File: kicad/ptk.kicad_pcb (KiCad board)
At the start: 2 copper layers, 121 x 87.8 mm, 18 parts

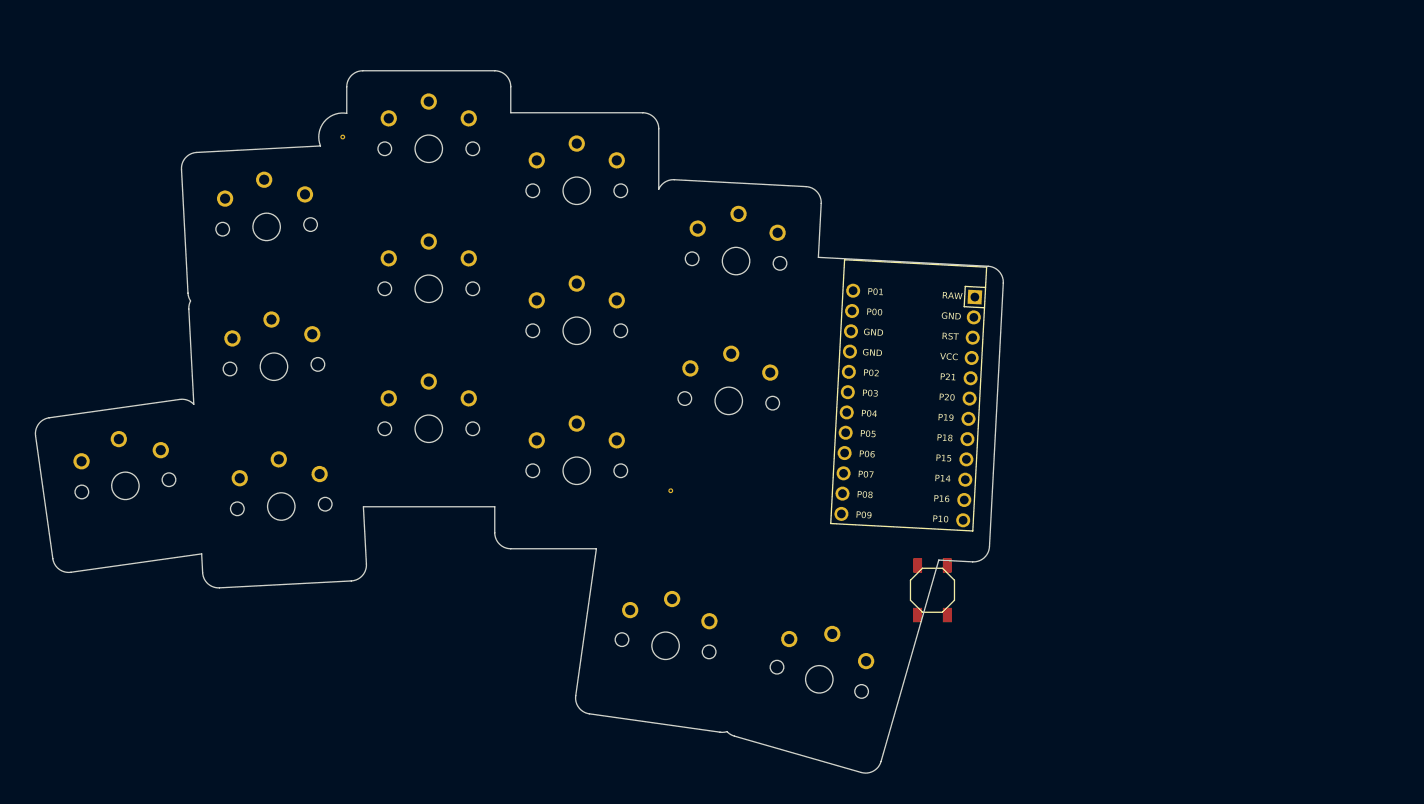
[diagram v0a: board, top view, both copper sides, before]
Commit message: updated schematic and footprints
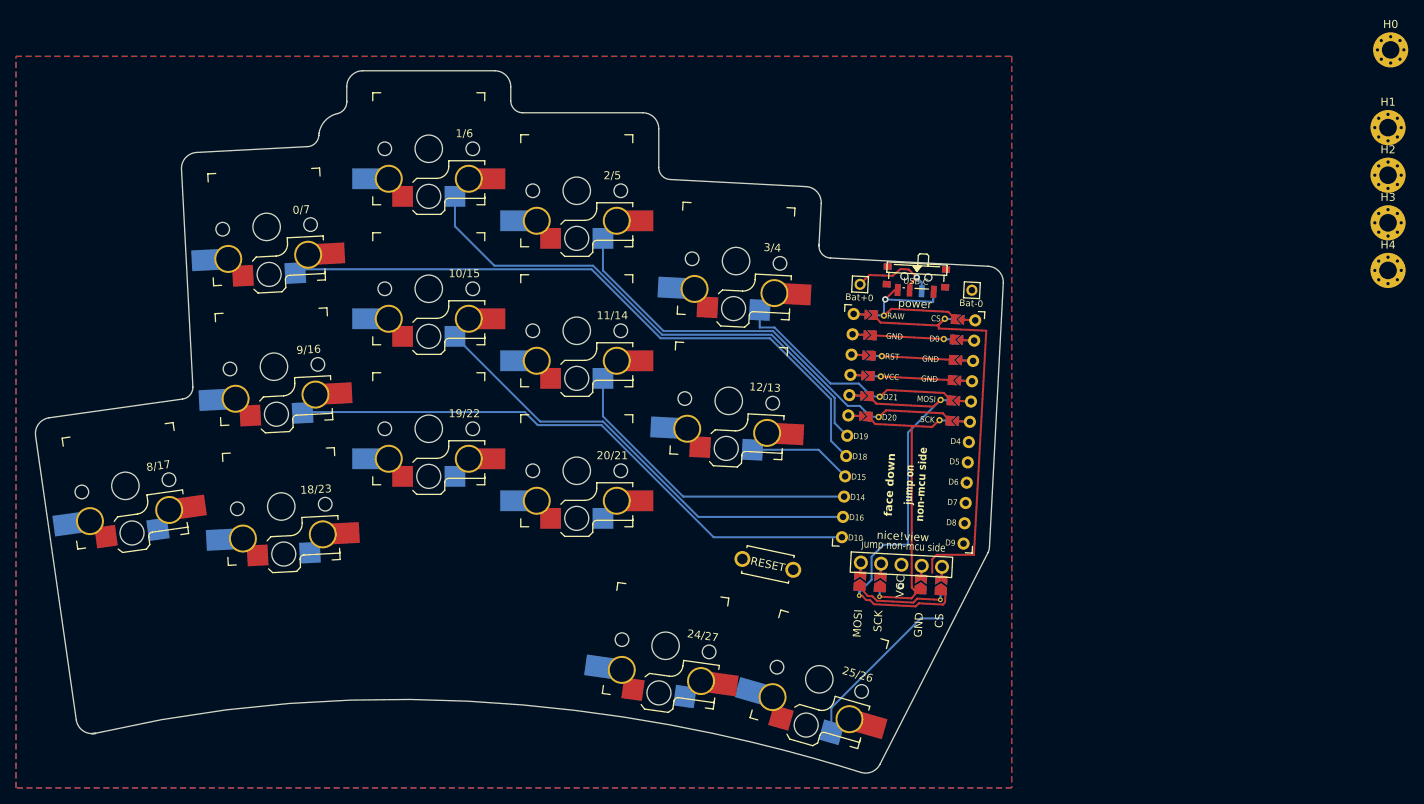
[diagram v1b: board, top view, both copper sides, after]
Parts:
- removed REF** (x2): VIA-0.6mm, VIA-0.6mm
- added Bat+0: MountingHole_Pad, keyboard:1pin_conn, F.Cu at (263.0, 114.9)
- added Bat-0: MountingHole_Pad, keyboard:1pin_conn, F.Cu at (277.0, 115.6)
- added H0: MountingHole_Pad, MountingHole:MountingHole_2.2mm_M2_Pad_Via, F.Cu at (329.3, 85.5)
- added H1: MountingHole_Pad, MountingHole:MountingHole_2.2mm_M2_Pad_Via, F.Cu at (329.0, 95.3)
- added H2: MountingHole_Pad, MountingHole:MountingHole_2.2mm_M2_Pad_Via, F.Cu at (329.0, 101.2)
- added H3: MountingHole_Pad, MountingHole:MountingHole_2.2mm_M2_Pad_Via, F.Cu at (329.0, 107.2)
- added H4: MountingHole_Pad, MountingHole:MountingHole_2.2mm_M2_Pad_Via, F.Cu at (329.0, 113.1)
- added J0: nice!view, chelming-kbd:nice-view_reversible, F.Cu at (269.0, 133.4)
- added RSW0: SW_Push, kbd:ResetSW, F.Cu at (251.5, 149.9)
- 0/7, 1/6, 10/15, 11/14, 12/13, 18/23, 19/22, 2/5, 20/21, 24/27, 25/26, 3/4, 8/17, 9/16: value (none) -> keyswitch; footprint PG1350 -> chelming-kbd:choc_v1_hotswap_reversible
- MCU0: renamed from MCU1; value (none) -> ProMicro-kbd; footprint ProMicro -> chelming-kbd:ProMicro_v3_nice_view_reversible
- SW_PWR0: renamed from B1; value (none) -> SW_SPST; footprint E73:SW_TACT_ALPS_SKQGABE010 -> chelming-kbd:SW_SPDT_PCM12_REVERSIBLE
- moved SW_PWR0 39.9 mm to (270.1, 113.2), turned to -3 degrees
- moved MCU0 3.42 mm to (269.0, 133.4), turned to -3 degrees
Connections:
- 0/7 pad 2: matrix_ring_top -> s0
- 1/6 pad 2: matrix_middle_top -> s1
- 10/15 pad 2: matrix_middle_home -> s10
- 11/14 pad 2: matrix_index_home -> s11
- 12/13 pad 2: matrix_inner_home -> s12
- 18/23 pad 2: matrix_ring_bottom -> s18
- 19/22 pad 2: matrix_middle_bottom -> s19
- 2/5 pad 2: matrix_index_top -> s2
- 20/21 pad 2: matrix_index_bottom -> s20
- 24/27 pad 2: thumb_tucky -> s24
- 25/26 pad 2: thumb_reachy -> s25
- 3/4 pad 2: matrix_inner_top -> s3
- 8/17 pad 2: matrix_pinky_home -> s8
- 9/16 pad 2: matrix_ring_home -> s9
- MCU0 pad 1: RAW -> cs
- MCU0 pad 10: matrix_middle_top -> s20
- MCU0 pad 11: matrix_middle_home -> s24
- MCU0 pad 12: matrix_middle_bottom -> s25
- MCU0 pad 13: P1 -> s9
- MCU0 pad 14: P0 -> s10
- MCU0 pad 15: GND -> s11
- MCU0 pad 16: GND -> s12
- MCU0 pad 17: P2 -> s0
- MCU0 pad 18: matrix_index_top -> s1
- MCU0 pad 19: matrix_index_home -> s2
- MCU0 pad 2: GND -> unconnected-(MCU0-RX-Pad2)_1
- MCU0 pad 20: matrix_index_bottom -> s3
- MCU0 pad 21: matrix_inner_top -> VCC
- MCU0 pad 22: matrix_inner_home -> reset
- MCU0 pad 23: thumb_reachy -> GND
- MCU0 pad 24: thumb_tucky -> raw
- MCU0 pad 3: RST -> GND
- MCU0 pad 4: VCC -> GND
- MCU0 pad 5: matrix_pinky_top -> mosi
- MCU0 pad 6: matrix_pinky_home -> sck
- MCU0 pad 7: matrix_ring_top -> s8
- MCU0 pad 8: matrix_ring_home -> s18
- MCU0 pad 9: matrix_ring_bottom -> s19
- SW_PWR0 pad 1: RST -> +BATT
- SW_PWR0 pad 2: GND -> raw
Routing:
- net s0: track 0.00 -> 81.8 mm
- net s9: track 0.00 -> 73.9 mm
- net s1: track 0.00 -> 65.5 mm
- net s10: track 0.00 -> 57.9 mm
- net s2: track 0.00 -> 45.0 mm
- net cs: track 0.00 -> 42.7 mm
- net s11: track 0.00 -> 39.0 mm
- net mosi: track 0.00 -> 30.5 mm
- net s25: track 0.00 -> 22.8 mm
- net sck: track 0.00 -> 21.3 mm
- net s3: track 0.00 -> 19.7 mm
- net s12: track 0.00 -> 13.0 mm
- net +BATT: track 0.00 -> 12.3 mm, vias 0 -> 1
- net raw: track 0.00 -> 11.4 mm, vias 0 -> 1
- net GND: vias 0 -> 1
- added copper zone on B.Cu, net GND
- added copper zone on F.Cu, net GND
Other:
- outline, holes or cut-outs redrawn

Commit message: add'l routing
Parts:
- removed H4: MountingHole_Pad, MountingHole:MountingHole_2.2mm_M2_Pad_Via
- moved H1 176.9 mm to (167.7, 167.9)
- moved H0 131.8 mm to (197.9, 96.2)
- moved H3 94.4 mm to (249.3, 157.8)
- moved H2 92.0 mm to (237.5, 111.0)
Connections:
- MCU0 pad 10: s20 -> s19
- MCU0 pad 13: s9 -> s8
- MCU0 pad 14: s10 -> s18
- MCU0 pad 15: s11 -> s20
- MCU0 pad 16: s12 -> s9
- MCU0 pad 17: s0 -> s11
- MCU0 pad 18: s1 -> s0
- MCU0 pad 7: s8 -> s1
- MCU0 pad 8: s18 -> s12
- MCU0 pad 9: s19 -> s10
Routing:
- net s8: track 0.00 -> 98.0 mm
- net s18: track 0.00 -> 72.5 mm
- net s19: track 0.00 -> 68.4 mm
- net s24: track 0.00 -> 48.7 mm
- net VCC: track 0.00 -> 44.5 mm
- net reset: track 0.00 -> 42.9 mm, vias 0 -> 4
- net s20: track 0.00 -> 30.4 mm
- net s10: track 57.9 -> 76.8 mm
- net s12: track 13.0 -> 31.6 mm
- net sck: track 21.3 -> 36.7 mm
- net s1: track 65.5 -> 80.8 mm
- net s25: track 22.8 -> 36.6 mm
- net mosi: track 30.5 -> 41.9 mm
- net s9: track 73.9 -> 70.8 mm
- net s0: track 81.8 -> 79.5 mm
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
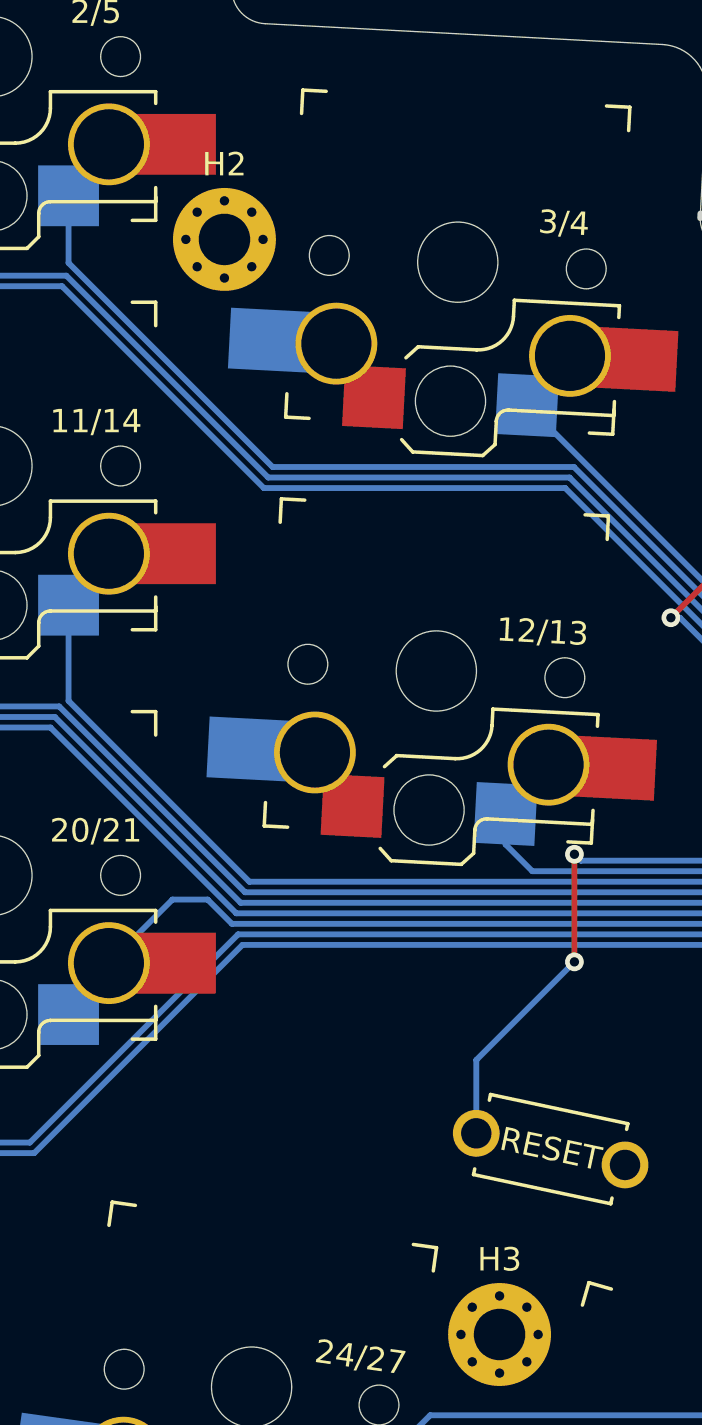
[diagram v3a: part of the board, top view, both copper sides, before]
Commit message: removing mounting hole
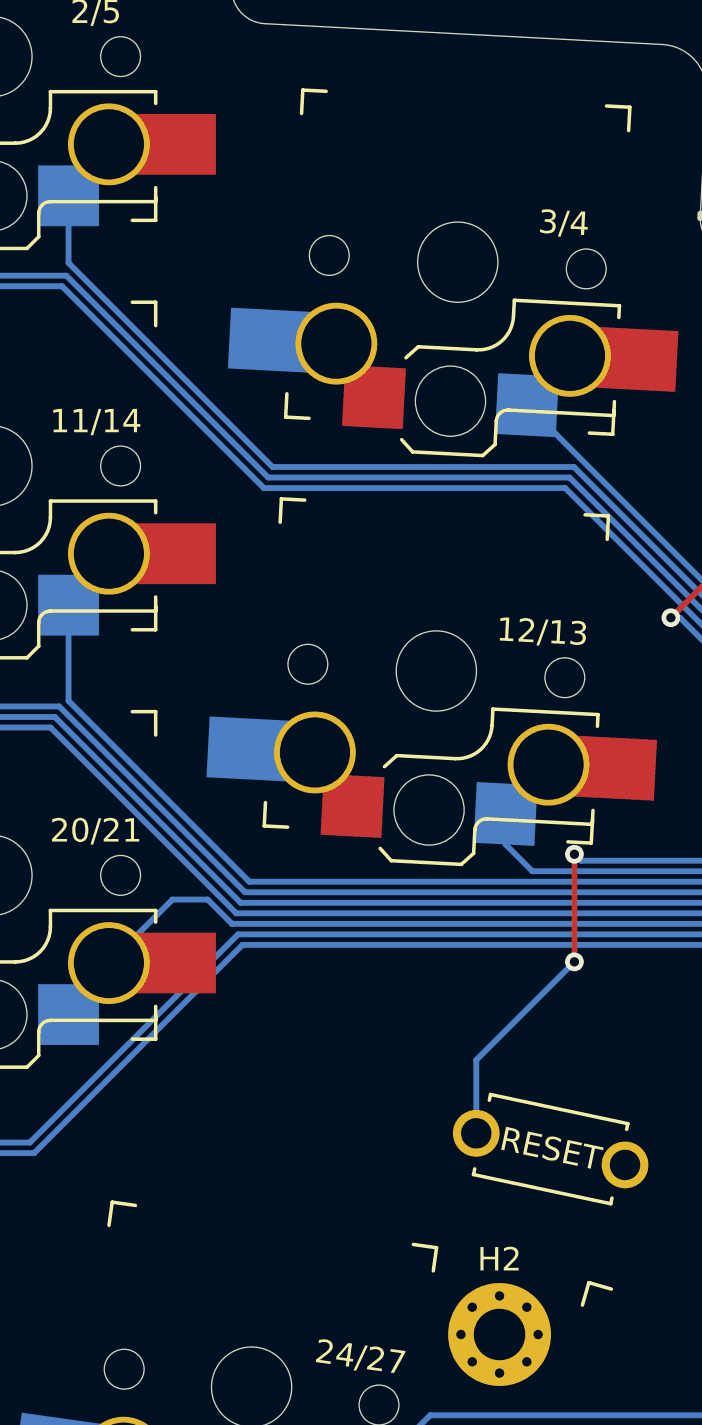
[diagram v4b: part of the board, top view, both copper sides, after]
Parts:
- removed the H2 at (237.5, 111.0)
- renumbered H3 to H2
